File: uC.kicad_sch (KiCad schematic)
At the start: 49 parts, among them J601 Conn_02x05_Counter_Clockwise, J602 Conn_02x08_Counter_Clockwise, J603 Conn_02x05_Counter_Clockwise, SW601 SW_Push, SW602 SW_Push, U601 STM32F103RGT6, U602 BLUENRG-M2SA, Y601 32.768KHz, Y602 16MHz

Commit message: only usb powered
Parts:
- renumbered C601 to C401, C602 to C402, C603 to C403, C604 to C404, C605 to C405, C606 to C406, C607 to C407, C608 to C408, C609 to C409, C610 to C410, C611 to C411, C612 to C412, C613 to C413, C614 to C414, C615 to C415, C616 to C416, C617 to C417, C618 to C418, C619 to C419, C620 to C420, C621 to C421, D601 to D401, D602 to D402, D603 to D403, D604 to D404, D605 to D405, D606 to D406, D607 to D407, D608 to D408, J601 to J401, J602 to J402, J603 to J403, L601 to L401, R601 to R401, R602 to R402, R603 to R403, R604 to R404, R605 to R405, R606 to R406, R607 to R407, R608 to R408, R609 to R409, R610 to R410, SW601 to SW401, SW602 to SW402, U601 to U401, U602 to U402, Y601 to Y401, Y602 to Y402
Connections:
- net uC_ADC_BATT is gone; now on net DAC_OUT1: U401.20 (PA4)
- net I2C1_SCL: now reaches J402.13 (Pin_13)
- net I2C1_SCL: now also U401.61 (PB8)
- net I2C1_SDA: now reaches J402.14 (Pin_14)
- net I2C1_SDA: now also U401.62 (PB9)
- net DAC_OUT1: now reaches J402.20 (Pin_20)
- net DCDC_2_EN: now reaches U401.33 (PB12)
- net BUTTON_PWR renamed LDO_EN
- net C_EN: no longer names the net of U401.24 (PC4)
- no-connect marks 18 -> 17
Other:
- moved on the sheet: C401, C402, J402

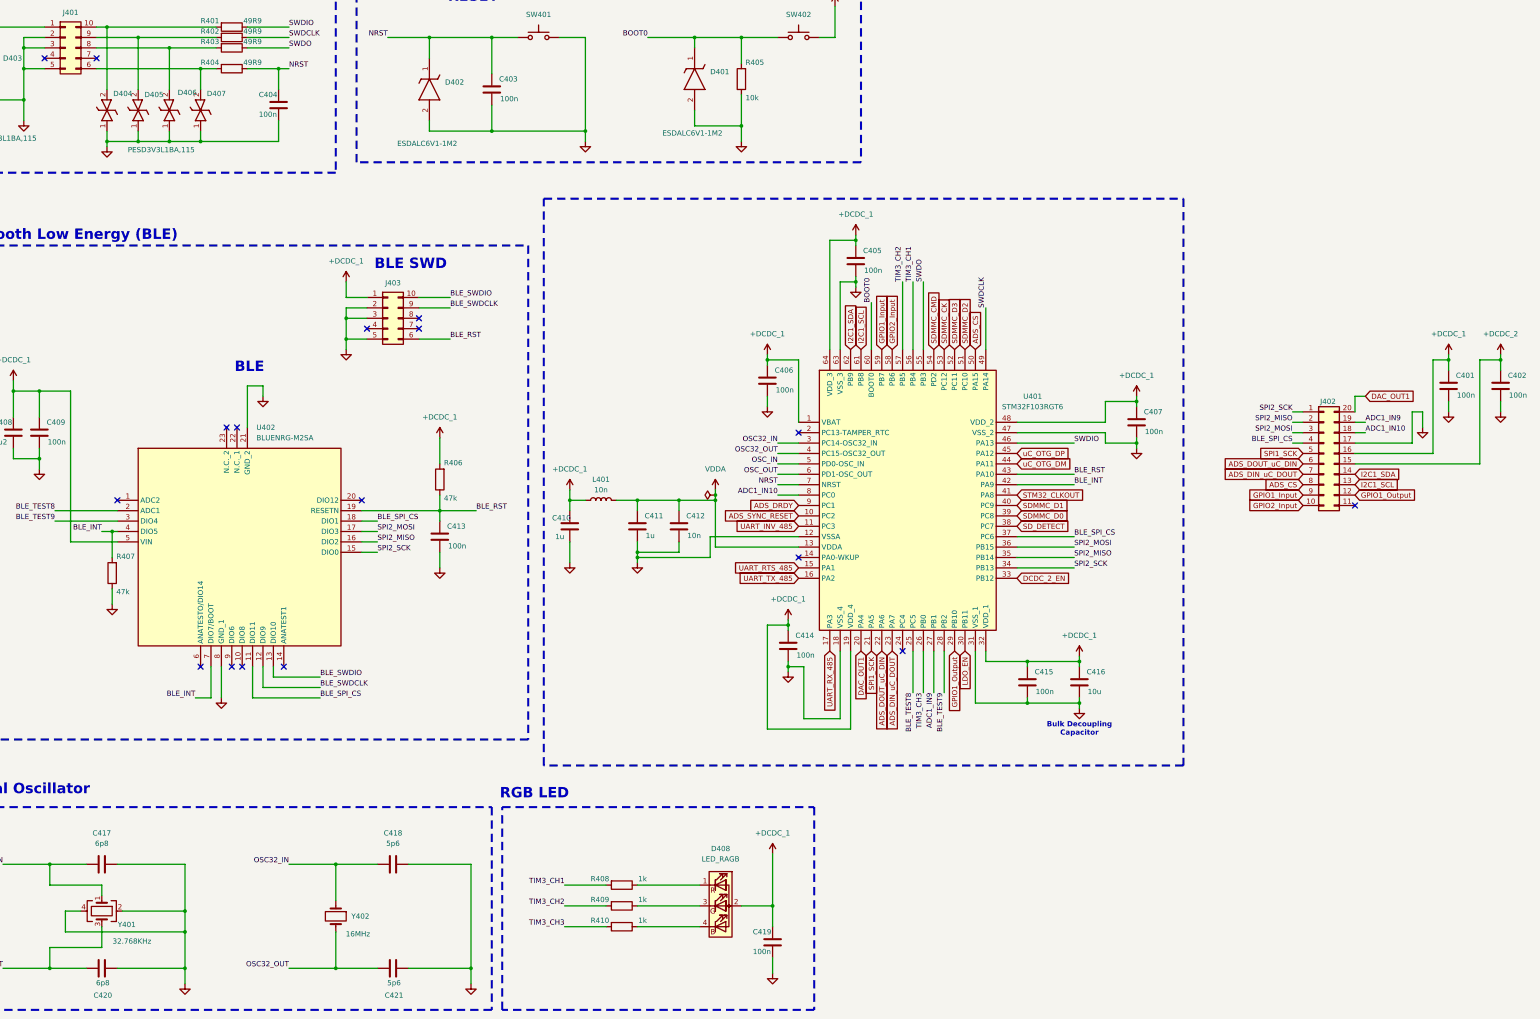
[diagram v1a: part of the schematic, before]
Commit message: components with distributor links added
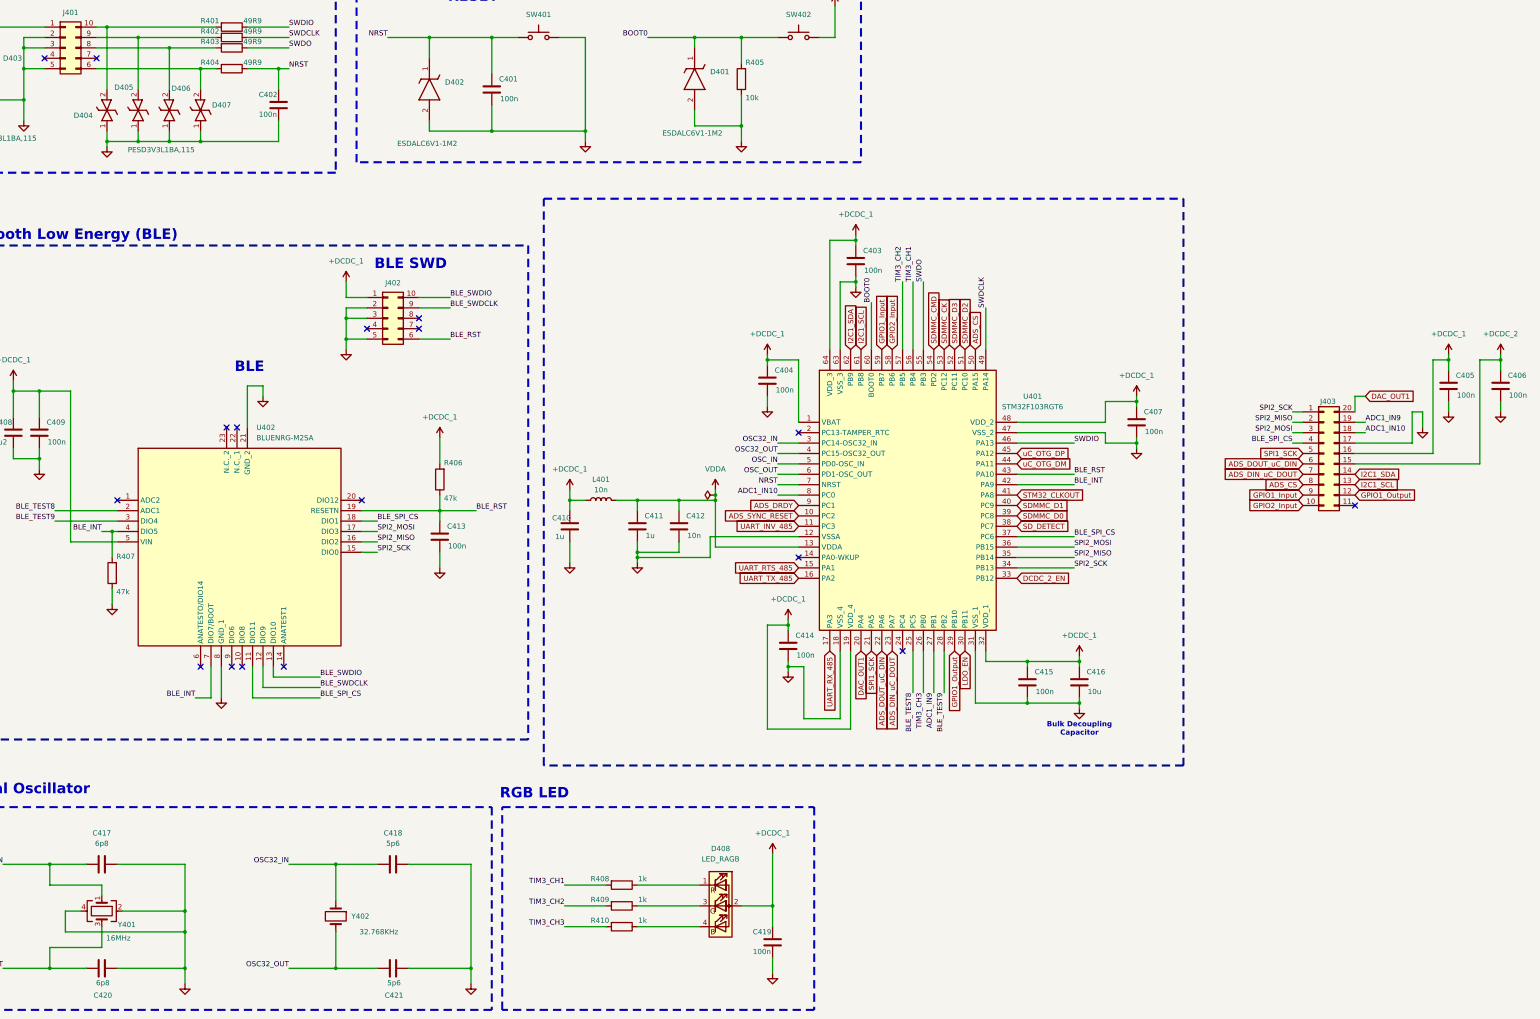
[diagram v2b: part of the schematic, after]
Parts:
- C401: renamed from C403; Distributor_Link (none) -> https://www.mouser.com/ProductDetail/KYOCERA-AVX/04023C104K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; Manufacturer_Name (none) -> KYOCERA AVX; Manufacturer_Part_Number (none) -> 04023C104KAT2A
- C402: renamed from C404; Distributor_Link (none) -> https://www.mouser.com/ProductDetail/KYOCERA-AVX/04023C104K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; Manufacturer_Name (none) -> KYOCERA AVX; Manufacturer_Part_Number (none) -> 04023C104KAT2A
- C403: renamed from C405; Distributor_Link (none) -> https://www.mouser.com/ProductDetail/KYOCERA-AVX/04023C104K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; Manufacturer_Name (none) -> KYOCERA AVX; Manufacturer_Part_Number (none) -> 04023C104KAT2A
- C404: renamed from C406; Distributor_Link (none) -> https://www.mouser.com/ProductDetail/KYOCERA-AVX/04023C104K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; Manufacturer_Name (none) -> KYOCERA AVX; Manufacturer_Part_Number (none) -> 04023C104KAT2A
- C405: renamed from C401; Distributor_Link (none) -> https://www.mouser.com/ProductDetail/KYOCERA-AVX/04023C104K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; Manufacturer_Name (none) -> KYOCERA AVX; Manufacturer_Part_Number (none) -> 04023C104KAT2A
- C406: renamed from C402; Distributor_Link (none) -> https://www.mouser.com/ProductDetail/KYOCERA-AVX/04023C104K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; Manufacturer_Name (none) -> KYOCERA AVX; Manufacturer_Part_Number (none) -> 04023C104KAT2A
- C407, C409, C413, C414, C415, C419: Distributor_Link (none) -> https://www.mouser.com/ProductDetail/KYOCERA-AVX/04023C104K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; Manufacturer_Name (none) -> KYOCERA AVX; Manufacturer_Part_Number (none) -> 04023C104KAT2A
- C408: Distributor_Link (none) -> https://www.mouser.com/ProductDetail/KYOCERA-AVX/KGM05AR51A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; Manufacturer_Name (none) -> KYOCERA AVX; Manufacturer_Part_Number (none) -> KGM05AR51A225KH
- C410, C411: Distributor_Link (none) -> https://www.mouser.com/ProductDetail/KYOCERA-AVX/KGM05AR70J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; Manufacturer_Name (none) -> KYOCERA AVX; Manufacturer_Part_Number (none) -> KGM05AR70J105KH
- C412: Distributor_Link (none) -> https://www.mouser.com/ProductDetail/KYOCERA-AVX/04026C103J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; Manufacturer_Name (none) -> KYOCERA AVX; Manufacturer_Part_Number (none) -> 04026C103JAT2A
- C416: footprint Capacitor_SMD:C_0402_1005Metric -> Capacitor_SMD:C_0603_1608Metric; Distributor_Link (none) -> https://www.mouser.com/ProductDetail/KYOCERA-AVX/KGM15CR51A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; Manufacturer_Name (none) -> KYOCERA AVX; Manufacturer_Part_Number (none) -> KGM15CR51A106KT
- C417, C420: Distributor_Link (none) -> https://www.mouser.com/ProductDetail/KYOCERA-AVX/04025A6R8G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; Manufacturer_Name (none) -> KYOCERA AVX; Manufacturer_Part_Number (none) -> 04025A6R8GAT2A
- C418, C421: Distributor_Link (none) -> https://www.mouser.com/ProductDetail/Murata-Electronics/GJM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; Manufacturer_Name (none) -> Murata Electronics; Manufacturer_Part_Number (none) -> GJM1555C1H5R6FB01D
- D401, D402: Distributor_Link (none) -> https://www.mouser.co.uk/ProductDetail/STMicroelectronics/E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
- D403, D404, D405, D406, D407: Distributor_Link (none) -> https://www.mouser.co.uk/ProductDetail/Nexperia/PESD3V3L1BA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
- D408: Distributor_Link (none) -> https://www.mouser.com/ProductDetail/Kingbright/APFA3010LSE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
- J401: Distributor_Link (none) -> https://www.mouser.com/ProductDetail/Wurth-Elektronik/62701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; Manufacturer_Name (none) -> Wurth Elektronik; Manufacturer_Part_Number (none) -> 62701021621
- J402: renamed from J403; Distributor_Link (none) -> https://www.mouser.com/ProductDetail/Wurth-Elektronik/62701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; Manufacturer_Name (none) -> Wurth Elektronik; Manufacturer_Part_Number (none) -> 62701021621
- J403: renamed from J402; Distributor_Link (none) -> https://www.mouser.com/ProductDetail/Harwin/M20-9720546?qs=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; Manufacturer_Name (none) -> Harwin; Manufacturer_Part_Number (none) -> M20-9720546
- L401: Distributor_Link (none) -> https://www.mouser.com/ProductDetail/ABRACON/AISC-0603HP-10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; Manufacturer_Name (none) -> ABRACON; Manufacturer_Part_Number (none) -> AISC-0603HP-10NJ-T
- R401, R402, R403, R404: Distributor_Link (none) -> https://www.mouser.com/ProductDetail/Vishay/M55342K11B49D9R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; Manufacturer_Name (none) -> Vishay; Manufacturer_Part_Number (none) -> M55342K11B49D9RS2
- R405: Distributor_Link (none) -> https://www.mouser.com/ProductDetail/Vishay-Dale/CRCW060310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; Manufacturer_Name (none) -> Vishay/Dale; Manufacturer_Part_Number (none) -> CRCW060310K0FKEI
- R406, R407: Distributor_Link (none) -> https://www.mouser.com/ProductDetail/Vishay-Dale/CRCW060347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; Manufacturer_Name (none) -> Vishay/Dale; Manufacturer_Part_Number (none) -> CRCW060347K0FKEAHP
- R408, R409, R410: Distributor_Link (none) -> https://www.mouser.com/ProductDetail/Vishay-Dale/CRCW06031K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; Manufacturer_Name (none) -> Vishay/Dale; Manufacturer_Part_Number (none) -> CRCW06031K00FKEE
- SW401, SW402: Distributor_Link (none) -> https://www.mouser.com/ProductDetail/CK/RS282G05A3SMRT?qs=G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; Manufacturer_Name (none) -> C&K; Manufacturer_Part_Number (none) -> RS282G05A3SMRT
- U401: Distributor_Link (none) -> https://www.mouser.co.uk/ProductDetail/STMicroelectronics/S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
- U402: Distributor_Link (none) -> https://www.mouser.co.uk/ProductDetail/STMicroelectronics/B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
- Y401: value 32.768KHz -> 16MHz; Distributor_Link (none) -> https://www.mouser.com/ProductDetail/NDK/NX3225GA-16.000M-S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
- Y402: value 16MHz -> 32.768KHz; Distributor_Link (none) -> https://www.mouser.com/ProductDetail/NDK/NX3215SA-32.768K-S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

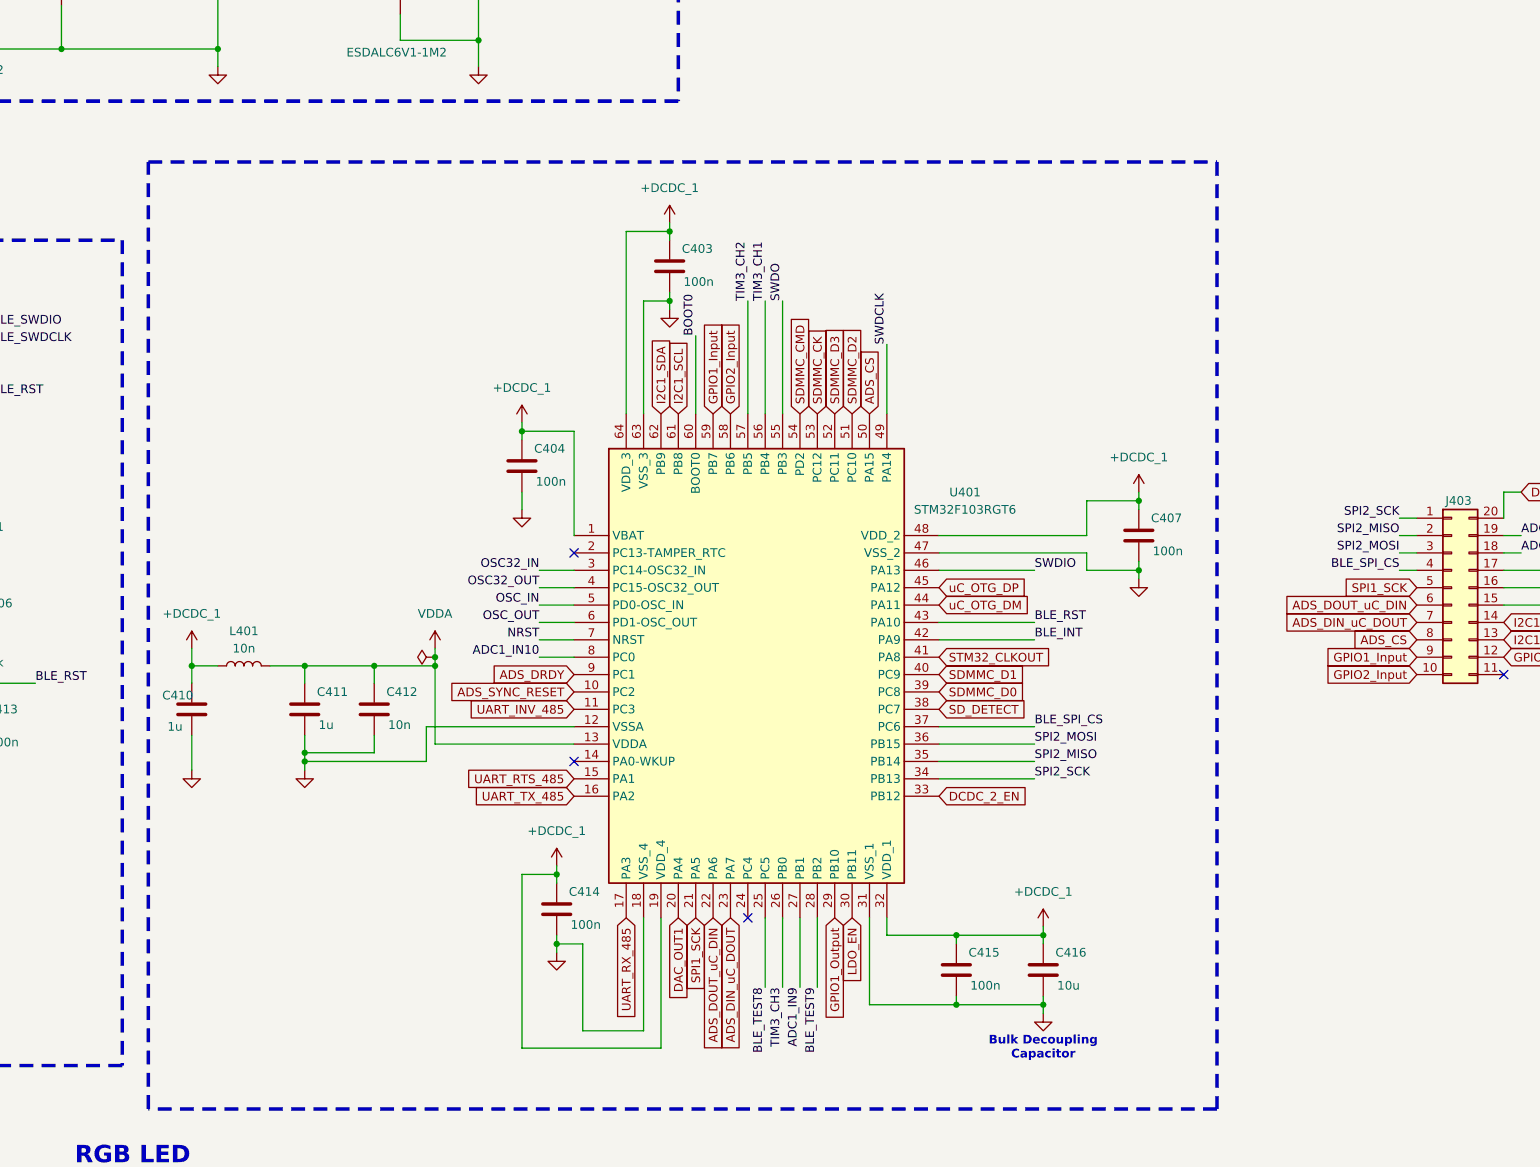
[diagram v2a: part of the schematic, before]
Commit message: minor improvements to net labeling
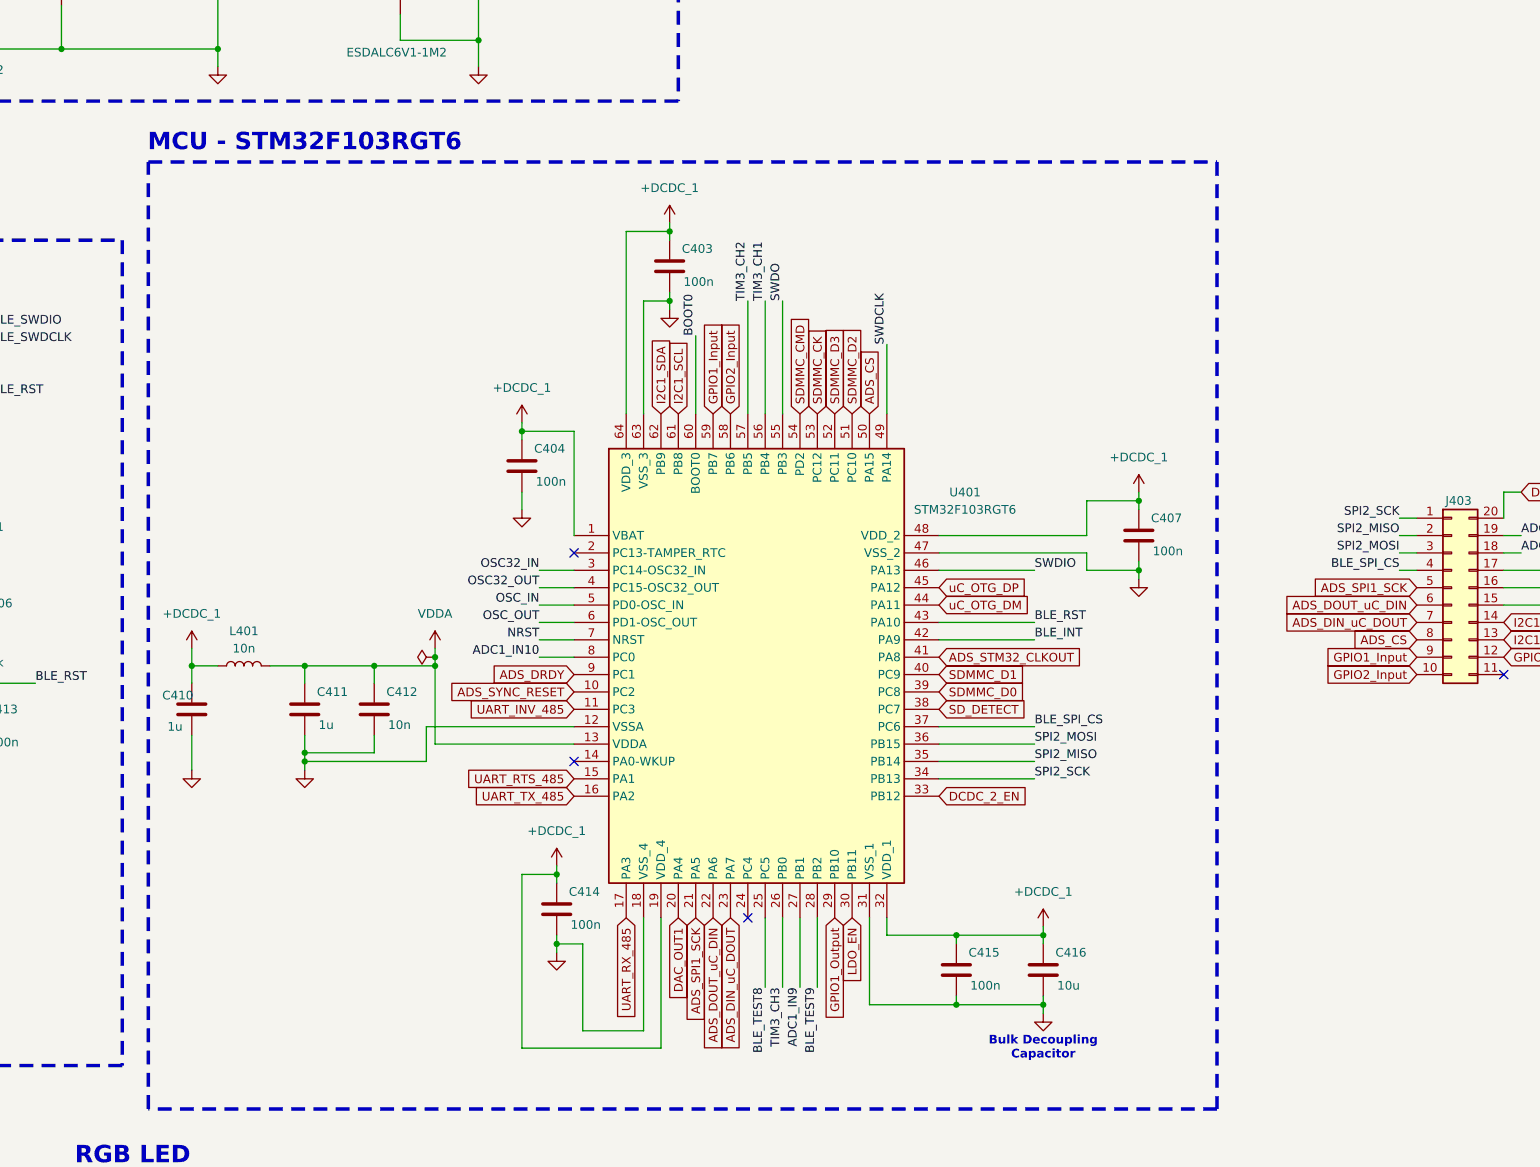
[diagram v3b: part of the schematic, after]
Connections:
- net SPI1_SCK renamed ADS_SPI1_SCK
- net STM32_CLKOUT renamed ADS_STM32_CLKOUT
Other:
- note added: "MCU - STM32F103RGT6"
